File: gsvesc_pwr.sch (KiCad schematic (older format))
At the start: 48 parts, among them J10 PHASE_C, J11 PHASE_B, J12 NTC, J9 PHASE_A, Q1 TPH2R608NH,L1Q, Q2 TPH2R608NH,L1Q, Q3 TPH2R608NH,L1Q, Q4 TPH2R608NH,L1Q, Q5 TPH2R608NH,L1Q, Q6 TPH2R608NH,L1Q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

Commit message: review
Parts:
- removed C50, C51, C52: 10u0/75V, Capacitor_SMD:C_1210_3225Metric, symbol Device:C
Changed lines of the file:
@@
 Wire Wire Line
 	2000 5500 2400 5500
-$Comp
-L Device:C C51
-U 1 1 5F2F1C49
-P 2850 1400
-F 0 "C51" H 2900 1500 50  0000 L CNN
-F 1 "10u0/75V" H 2700 1300 50  0000 L CNN
-F 2 "Capacitor_SMD:C_1210_3225Metric" H 2888 1250 50  0001 C CNN
-F 3 "~" H 2850 1400 50  0001 C CNN
-	1    2850 1400
-	1    0    0    -1
-$EndComp
-Wire Wire Line
-	2850 850  2850 1250
-Wire Wire Line
-	2850 1550 2850 2250
-Wire Wire Line
-	2450 850  2850 850
-Wire Wire Line
-	2450 2250 2850 2250
-Connection ~ 2450 850
-Connection ~ 2450 2250
-Wire Wire Line
-	1750 1600 3150 1600
 Wire Wire Line
 	2050 3050 2500 3050
 Wire Wire Line
 	2050 4450 2500 4450
-$Comp
-L Device:C C52
-U 1 1 5F31C9E5
-P 2950 3500
-F 0 "C52" H 3000 3600 50  0000 L CNN
-F 1 "10u0/75V" H 2800 3400 50  0000 L CNN
-F 2 "Capacitor_SMD:C_1210_3225Metric" H 2988 3350 50  0001 C CNN
-F 3 "~" H 2950 3500 50  0001 C CNN
-	1    2950 3500
-	1    0    0    -1
-$EndComp
-Wire Wire Line
-	2950 3050 2950 3350
-Wire Wire Line
-	2950 3650 2950 4450
-Wire Wire Line
-	2500 3050 2950 3050
-Wire Wire Line
-	2500 4450 2950 4450
-Connection ~ 2500 3050
-Connection ~ 2500 4450
 Wire Wire Line
 	3550 3800 3850 3800
 Wire Wire Line
 	1750 3800 3150 3800
-$Comp
-L Device:C C50
-U 1 1 5F33DFA1
-P 2800 5950
-F 0 "C50" H 2850 6050 50  0000 L CNN
-F 1 "10u0/75V" H 2650 5850 50  0000 L CNN
-F 2 "Capacitor_SMD:C_1210_3225Metric" H 2838 5800 50  0001 C CNN
-F 3 "~" H 2800 5950 50  0001 C CNN
-	1    2800 5950
-	1    0    0    -1
-$EndComp
-Wire Wire Line
-	2800 5500 2800 5800
-Wire Wire Line
-	2800 6100 2800 6900
-Wire Wire Line
-	2400 6900 2800 6900
-Wire Wire Line
-	2400 5500 2800 5500
-Connection ~ 2400 5500
-Connection ~ 2400 6900
 Wire Wire Line
 	1700 6250 3050 6250
@@
 	3200 1600 3150 1600
 Connection ~ 3150 1600
+Wire Wire Line
+	1750 1600 3150 1600
 $EndSCHEMATC

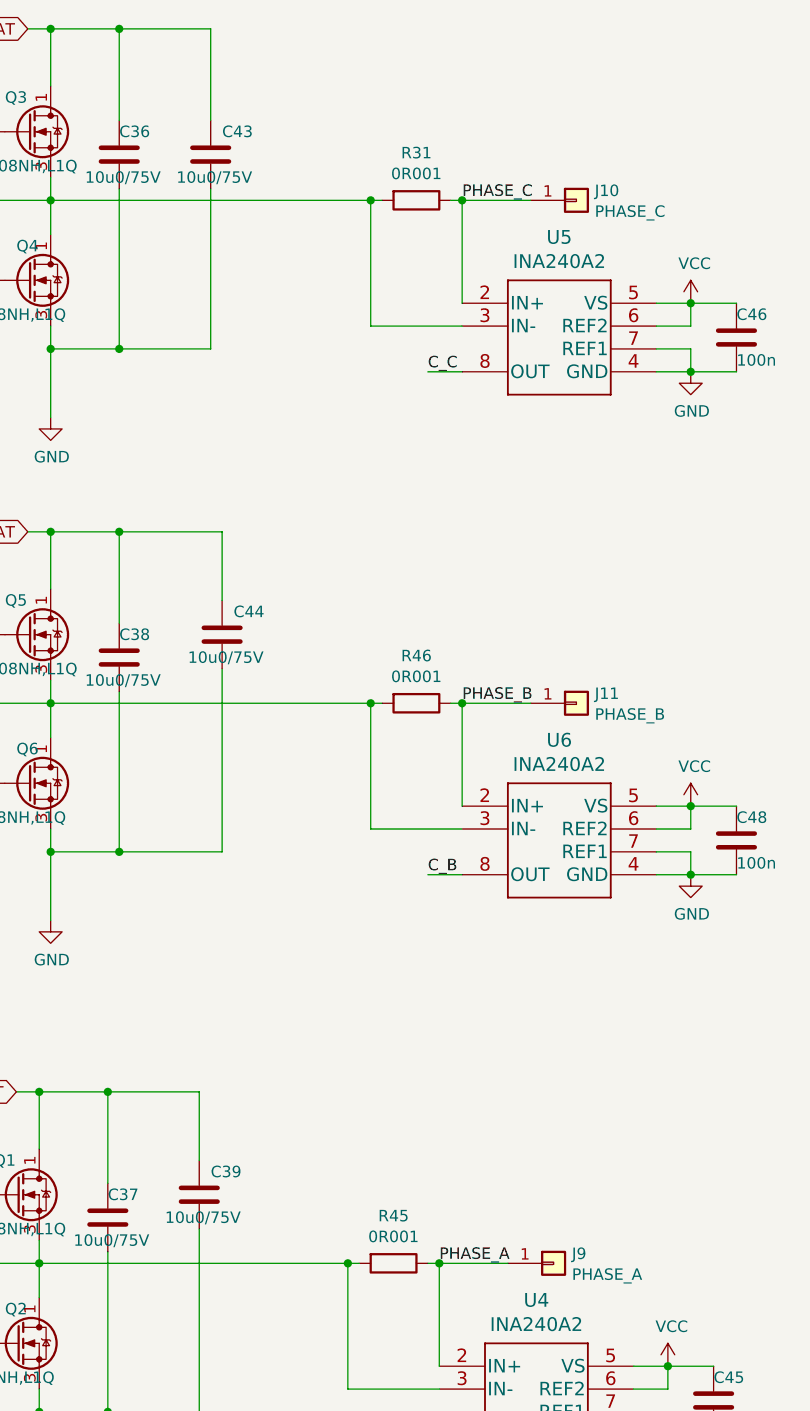
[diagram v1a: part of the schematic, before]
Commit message: current range too small, fix with new Shunt Resistor
!! better: use ina240A1
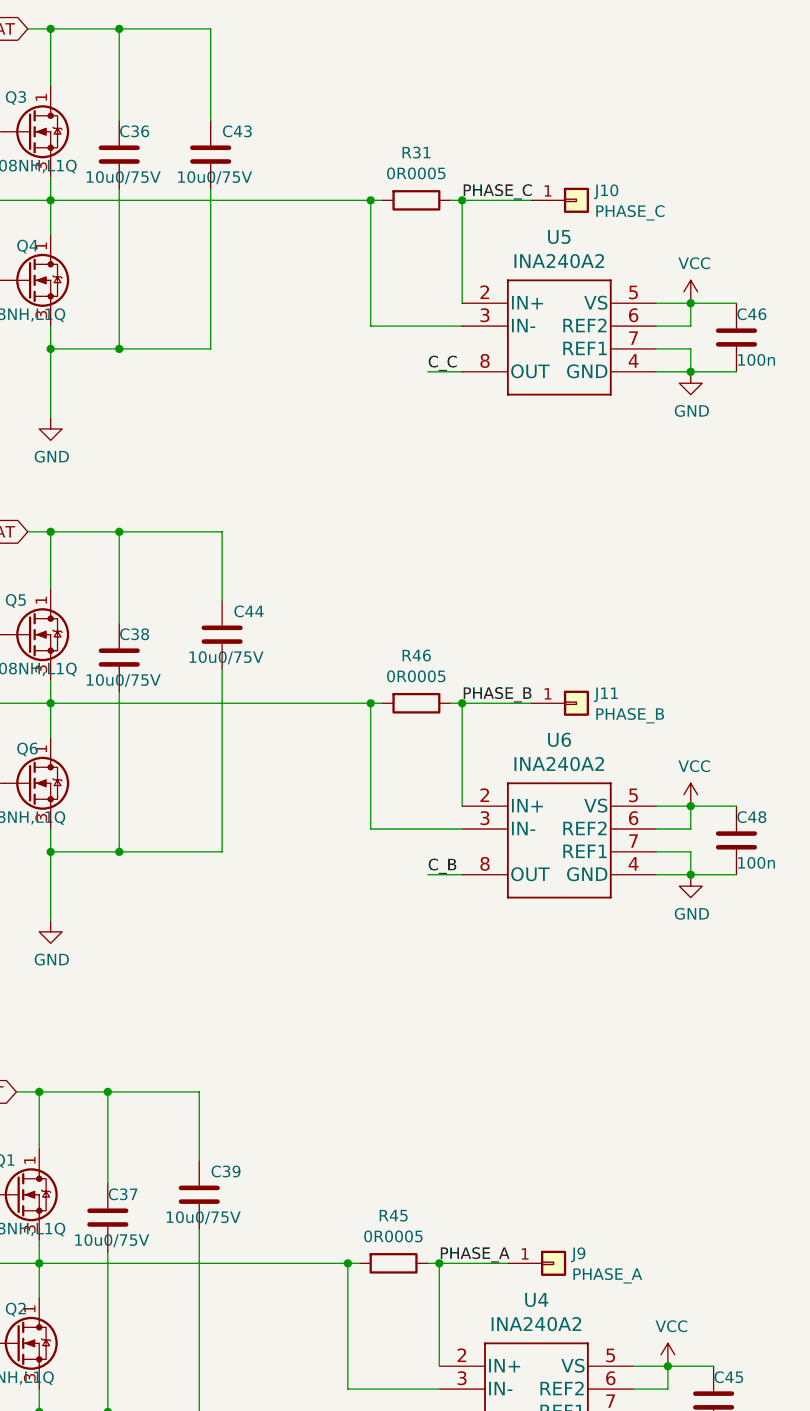
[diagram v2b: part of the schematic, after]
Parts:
- R31, R45, R46: value 0R001 -> 0R0005
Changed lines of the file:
@@
 P 3350 1600
 F 0 "R31" V 3143 1600 50  0000 C CNN
-F 1 "0R001" V 3234 1600 50  0000 C CNN
+F 1 "0R0005" V 3234 1600 50  0000 C CNN
 F 2 "Resistor_SMD:R_2512_6332Metric" V 3280 1600 50  0001 C CNN
 F 3 "~" H 3350 1600 50  0001 C CNN
@@
 P 3350 3800
 F 0 "R46" V 3143 3800 50  0000 C CNN
-F 1 "0R001" V 3234 3800 50  0000 C CNN
+F 1 "0R0005" V 3234 3800 50  0000 C CNN
 F 2 "Resistor_SMD:R_2512_6332Metric" V 3280 3800 50  0001 C CNN
 F 3 "~" H 3350 3800 50  0001 C CNN
@@
 P 3250 6250
 F 0 "R45" V 3043 6250 50  0000 C CNN
-F 1 "0R001" V 3134 6250 50  0000 C CNN
+F 1 "0R0005" V 3134 6250 50  0000 C CNN
 F 2 "Resistor_SMD:R_2512_6332Metric" V 3180 6250 50  0001 C CNN
 F 3 "~" H 3250 6250 50  0001 C CNN
